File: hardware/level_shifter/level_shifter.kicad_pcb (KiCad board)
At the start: 2 copper layers, 45.5 x 48.5 mm, 25 parts, among them J1 Conn_01x04, J2 Conn_01x04, J3 Conn_01x02, J4 Conn_01x02, J5 Conn_01x02, J6 Conn_01x02, Q1 2N7000, Q2 2N7000, Q3 2N7000, Q4 2N7000

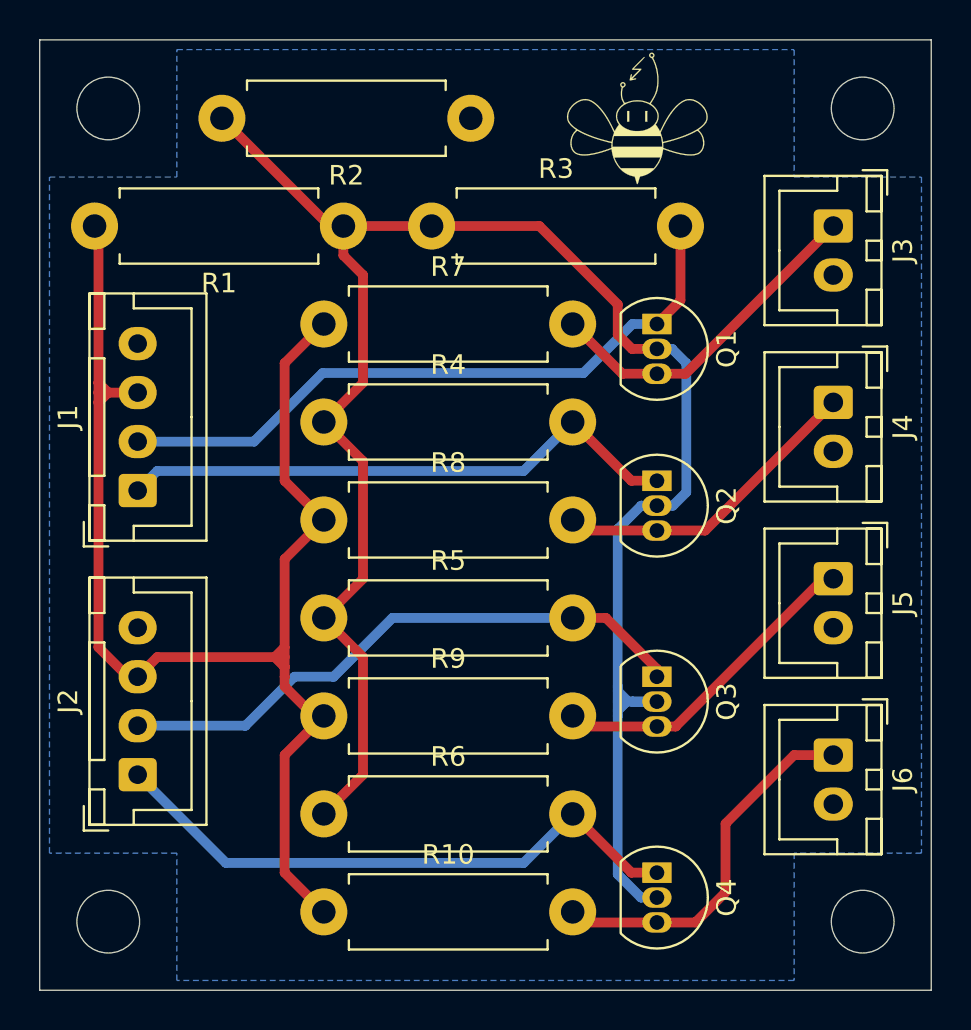
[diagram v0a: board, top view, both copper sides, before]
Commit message: Add gerbers and screenshots
Added gerber files, screenshots and updated silkscreen
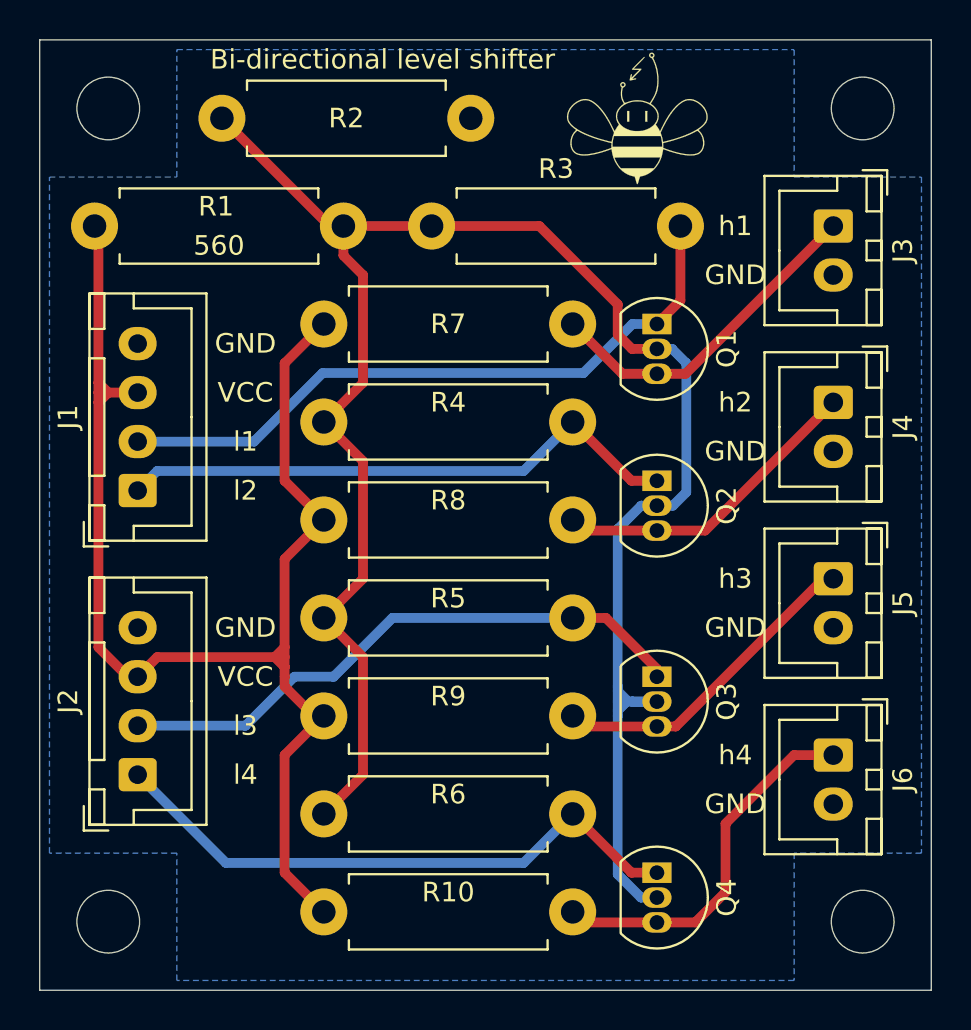
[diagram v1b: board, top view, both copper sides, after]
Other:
- board text added: "Bi-directional level shifter"
- board text added: "GND"
- board text added: "VCC"
- board text added: "h1"
- board text added: "h2"
- board text added: "h3"
- board text added: "h4"
- board text added: "l1"
- board text added: "l2"
- board text added: "l3"
- board text added: "l4"

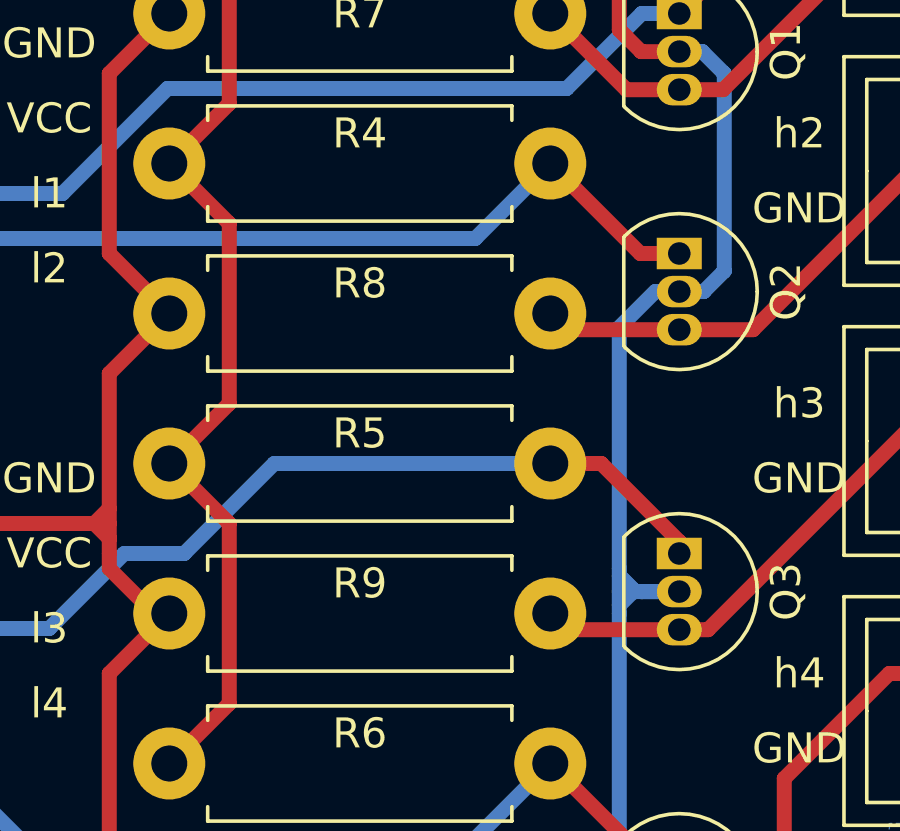
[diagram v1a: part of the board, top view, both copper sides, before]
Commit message: Apply CERN-W license
Apply CERN-W license to all boards, move the first iteration of the IR_sensor to the archive

Co-Authored-By: Andre Maia Chagas <a.maia-chagas@sussex.ac.uk>
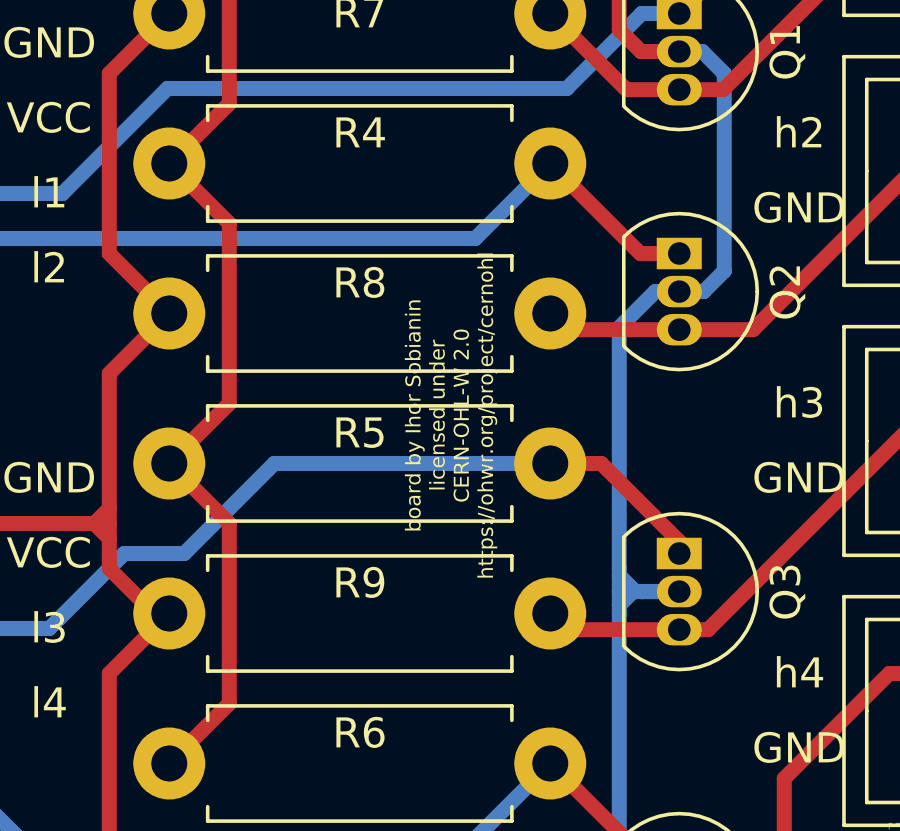
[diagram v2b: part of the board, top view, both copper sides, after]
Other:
- board text added: "board by Ihor Sobianin licensed under CERN-OHL-W 2.0 https://ohwr.org/project/cernohl"

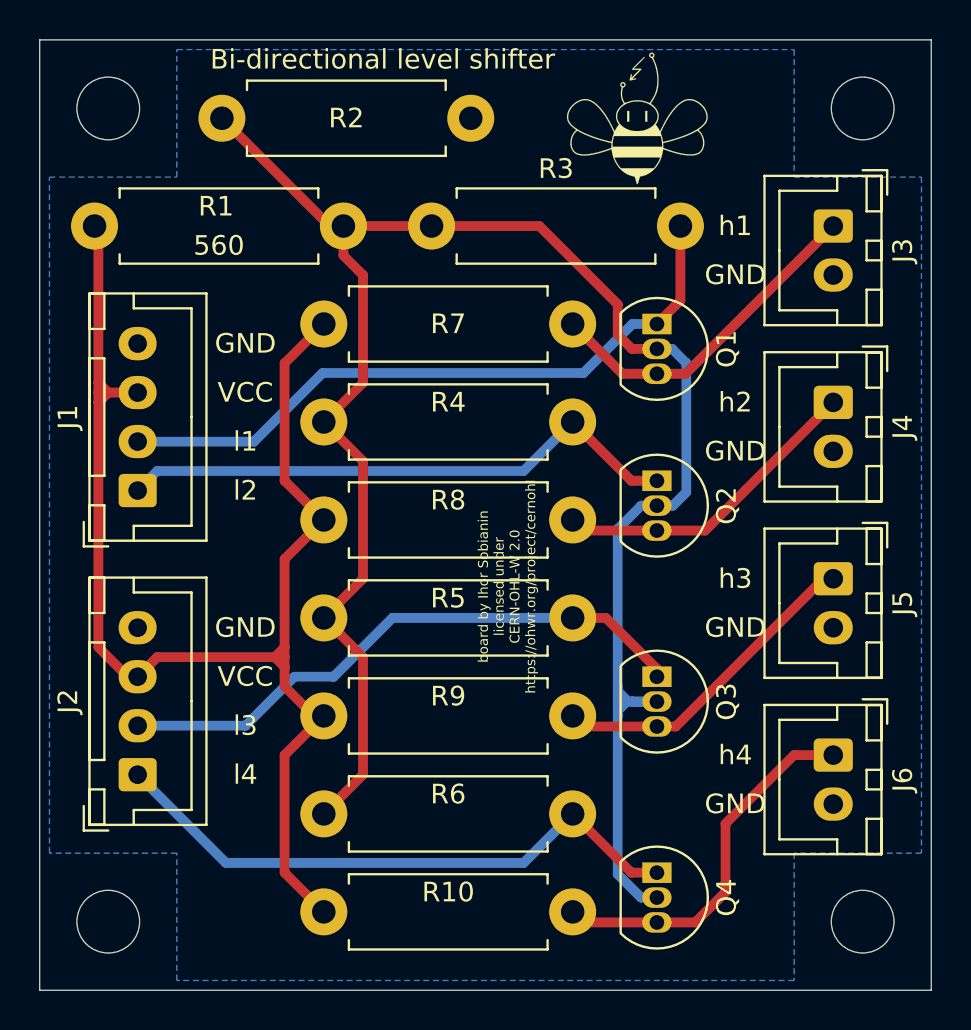
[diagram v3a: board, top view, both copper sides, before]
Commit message: update to92 connector in level shifter
it is now a wide footprint, which should be easier to solder
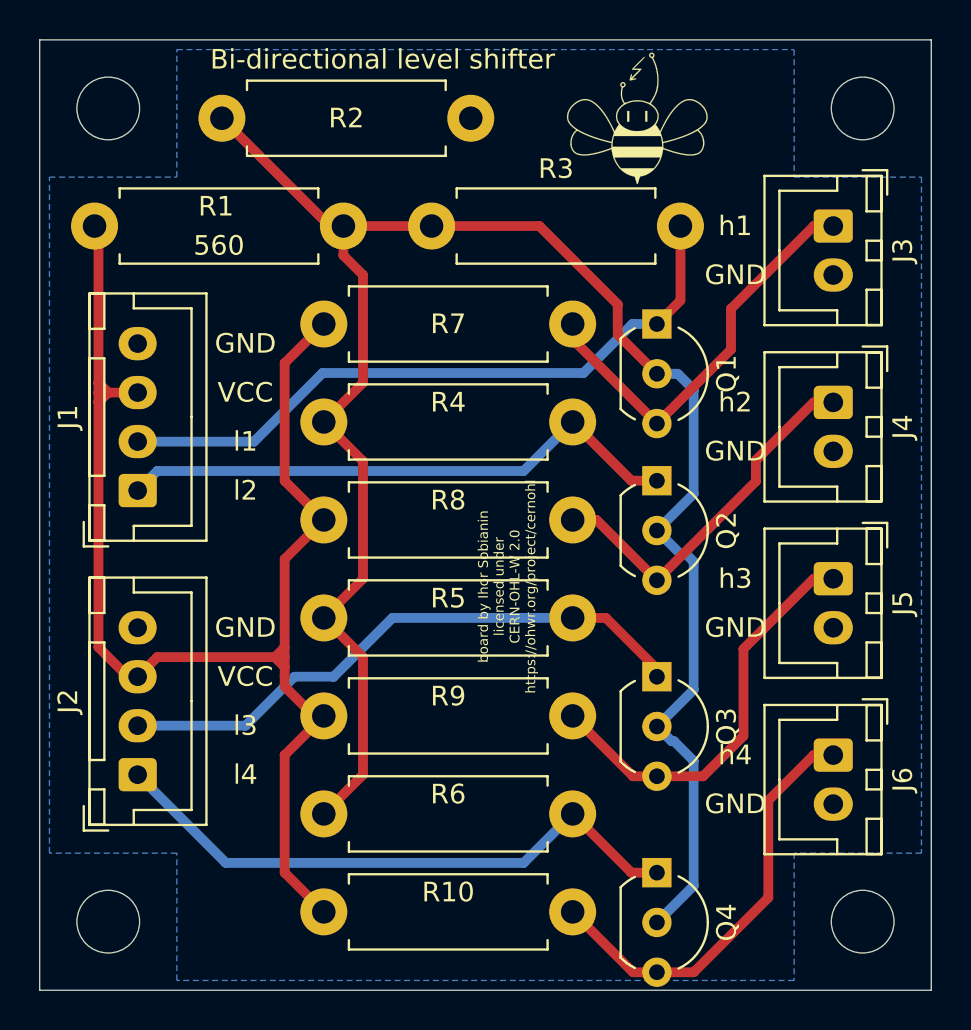
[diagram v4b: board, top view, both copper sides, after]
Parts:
- Q1, Q2, Q3, Q4: footprint Package_TO_SOT_THT:TO-92_Inline -> Package_TO_SOT_THT:TO-92_Inline_Wide
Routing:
- net d3_h: track 16.6 -> 21.3 mm
- net d1_h: track 17.5 -> 21.3 mm
- net +3V3: track 100.0 -> 96.6 mm
- net d4_h: track 19.1 -> 22.1 mm
- net d2_h: track 16.2 -> 19.0 mm
